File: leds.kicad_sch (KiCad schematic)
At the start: 11 parts

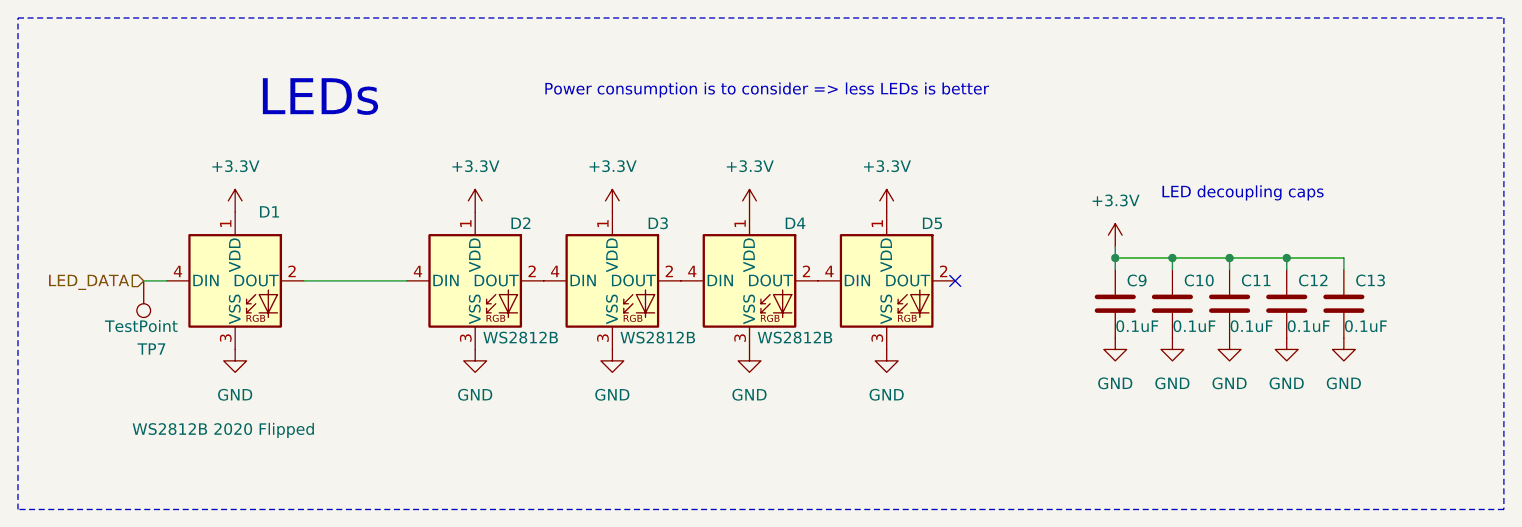
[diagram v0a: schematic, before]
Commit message: remove ATTiny; fix LED footprints; start cleanup
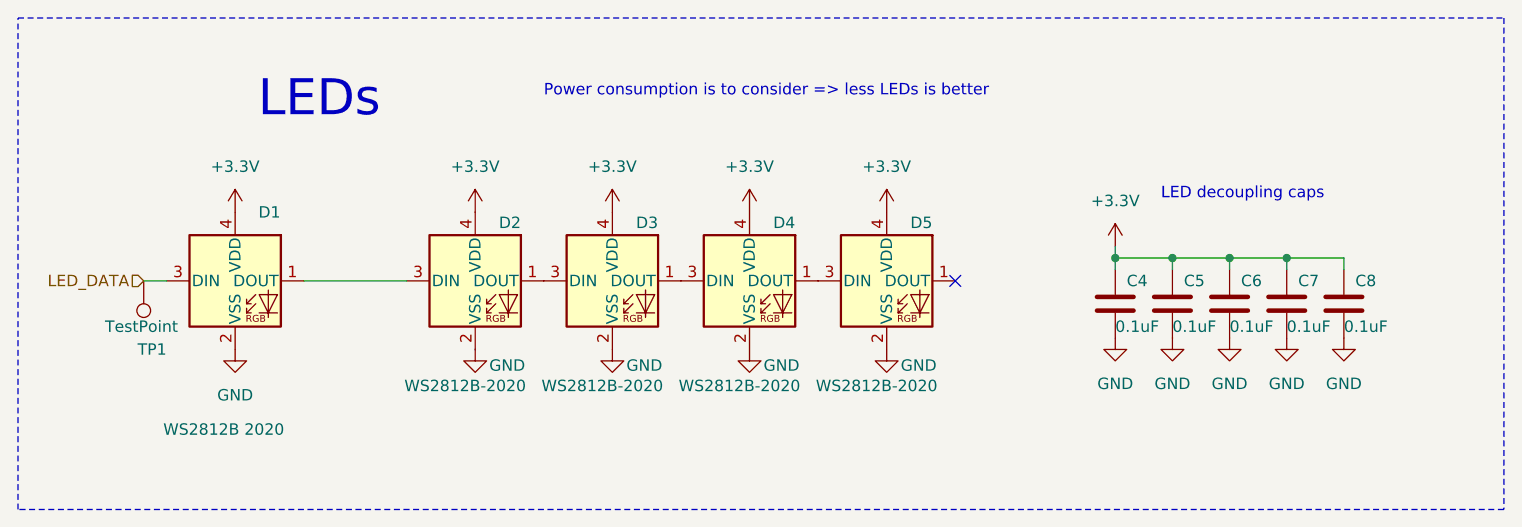
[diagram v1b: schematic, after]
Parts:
- D1: value WS2812B 2020 Flipped -> WS2812B 2020
- D2, D3, D4, D5: value WS2812B -> WS2812B-2020; symbol LED:WS2812B -> LED:WS2812B-2020
- renumbered C9 to C4, C10 to C5, C11 to C6, C12 to C7, C13 to C8, TP7 to TP1
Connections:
- net +3.3V: now also D1.4 (VDD), D2.4 (VDD), D3.4 (VDD), D4.4 (VDD), D5.4 (VDD); no longer D1.1 (VDD), D2.1 (VDD), D3.1 (VDD), D4.1 (VDD), D5.1 (VDD)
- net GND: now also D1.2 (VSS), D2.2 (VSS), D3.2 (VSS), D4.2 (VSS), D5.2 (VSS); no longer D1.3 (VSS), D2.3 (VSS), D3.3 (VSS), D4.3 (VSS), D5.3 (VSS)
- net LED_DATA: now also D1.3 (DIN); no longer D1.4 (DIN)
- new net: D1.1 (DOUT), D2.3 (DIN)
- new net: D4.1 (DOUT), D5.3 (DIN)
- new net: D3.1 (DOUT), D4.3 (DIN)
- new net: D2.1 (DOUT), D3.3 (DIN)

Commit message: change pressure bridge to four DMS
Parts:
- TP1: footprint TestPoint:TestPoint_Pad_D3.0mm -> TestPoint:TestPoint_Pad_D2.0mm
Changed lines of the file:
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@@
 			)
 		)
-		(property "Footprint" "TestPoint:TestPoint_Pad_D3.0mm"
+		(property "Footprint" "TestPoint:TestPoint_Pad_D2.0mm"
 			(at 54.61 62.23 0)
 			(effects
@@
 			(at 59.69 62.23 0)
 			(effects
+				(font
+					(size 1.27 1.27)
+				)
+				(hide yes)
+			)
+		)
+		(property "mpn" ""
+			(at 59.69 62.23 0)
+			(effects
